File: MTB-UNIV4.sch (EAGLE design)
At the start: 116 parts, among them IC1 MEGA128-A, IC2 SN75176BP, IC3 MC7805CDTG, IC4 ULN2803A, IC5 ULN2803A, Q1 14.745 MHz, X1A MVE252-5-V, X1B MVE252-5-V, X2A MVE252-5-V, X2B MVE252-5-V, X3 1751316, X4 1751316, X5 1751316, X6 1751316

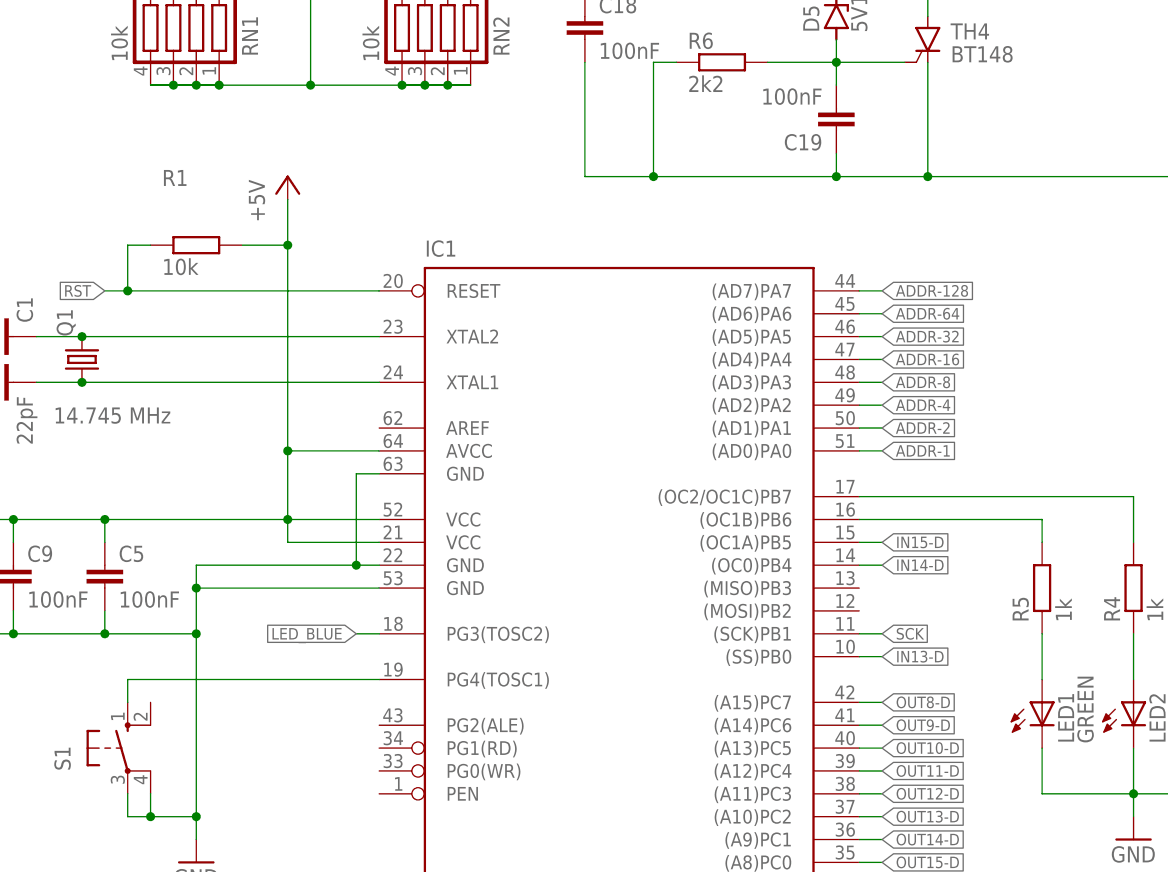
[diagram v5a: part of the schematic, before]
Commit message: Add test pads for MOSI & MISO.
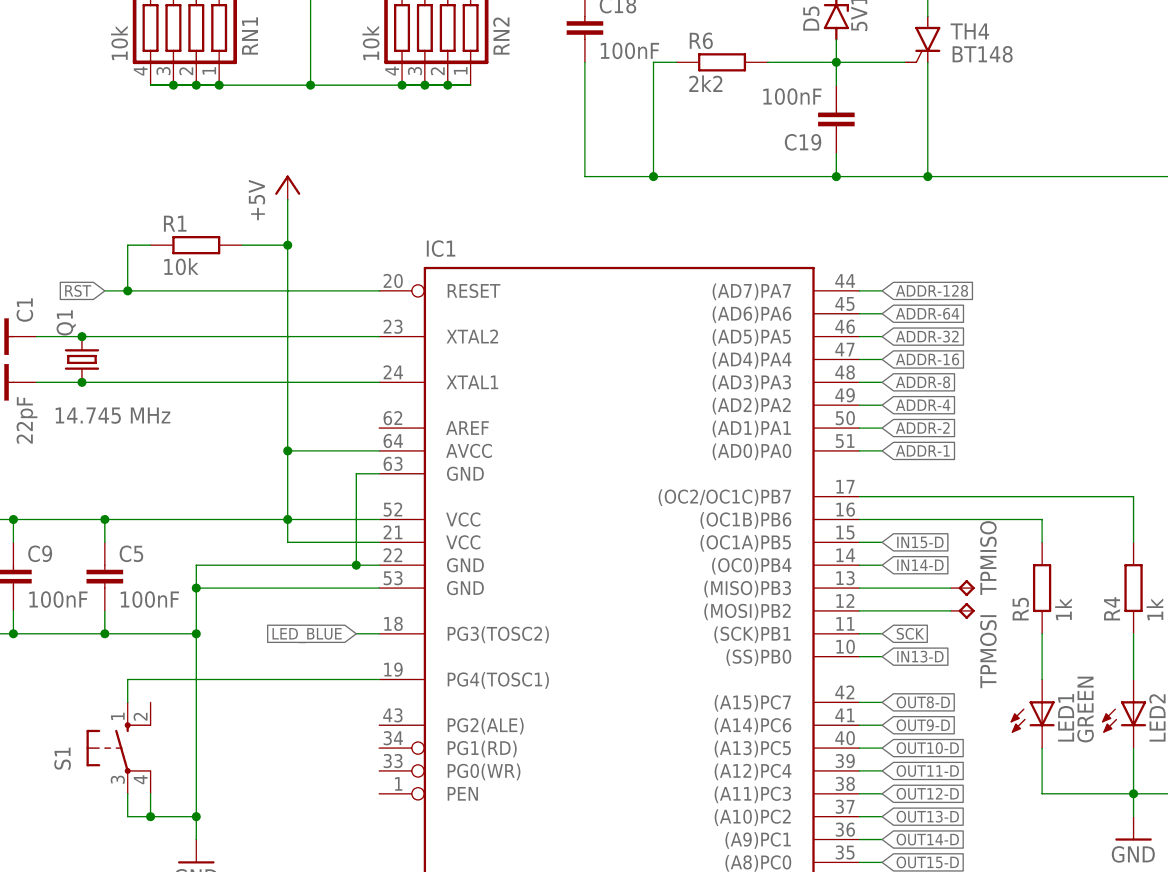
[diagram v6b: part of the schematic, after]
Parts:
- added TPMISO, TPMOSI: TPTP10R, testpad:TPTP10R
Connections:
- new net MISO: IC1.(MISO)PB3, TPMISO.TP
- new net MOSI: IC1.(MOSI)PB2, TPMOSI.TP
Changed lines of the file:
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@@
 <grid distance="0.1" unitdist="inch" unit="inch" style="lines" multiple="1" display="no" altdistance="0.01" altunitdist="inch" altunit="inch"/>
 <layers>
-<layer number="1" name="Top" color="3" fill="1" visible="yes" active="no"/>
-<layer number="2" name="Route2" color="1" fill="3" visible="yes" active="no"/>
-<layer number="3" name="Route3" color="4" fill="3" visible="yes" active="no"/>
-<layer number="4" name="Route4" color="1" fill="4" visible="yes" active="no"/>
-<layer number="5" name="Route5" color="4" fill="4" visible="yes" active="no"/>
-<layer number="6" name="Route6" color="1" fill="8" visible="yes" active="no"/>
-<layer number="7" name="Route7" color="4" fill="8" visible="yes" active="no"/>
-<layer number="8" name="Route8" color="1" fill="2" visible="yes" active="no"/>
-<layer number="9" name="Route9" color="4" fill="2" visible="yes" active="no"/>
-<layer number="10" name="Route10" color="1" fill="7" visible="yes" active="no"/>
-<layer number="11" name="Route11" color="4" fill="7" visible="yes" active="no"/>
-<layer number="12" name="Route12" color="1" fill="5" visible="yes" active="no"/>
-<layer number="13" name="Route13" color="4" fill="5" visible="yes" active="no"/>
-<layer number="14" name="Route14" color="1" fill="6" visible="yes" active="no"/>
-<layer number="15" name="Route15" color="4" fill="6" visible="yes" active="no"/>
-<layer number="16" name="Bottom" color="4" fill="1" visible="yes" active="no"/>
-<layer number="17" name="Pads" color="2" fill="1" visible="yes" active="no"/>
-<layer number="18" name="Vias" color="2" fill="1" visible="yes" active="no"/>
-<layer number="19" name="Unrouted" color="6" fill="1" visible="yes" active="no"/>
-<layer number="20" name="Dimension" color="24" fill="1" visible="yes" active="no"/>
-<layer number="21" name="tPlace" color="7" fill="1" visible="yes" active="no"/>
-<layer number="22" name="bPlace" color="7" fill="1" visible="yes" active="no"/>
-<layer number="23" name="tOrigins" color="15" fill="1" visible="yes" active="no"/>
-<layer number="24" name="bOrigins" color="15" fill="1" visible="yes" active="no"/>
-<layer number="25" name="tNames" color="7" fill="1" visible="yes" active="no"/>
-<layer number="26" name="bNames" color="7" fill="1" visible="yes" active="no"/>
-<layer number="27" name="tValues" color="7" fill="1" visible="yes" active="no"/>
-<layer number="28" name="bValues" color="7" fill="1" visible="yes" active="no"/>
+<layer number="1" name="Top" color="3" fill="1" visible="no" active="no"/>
+<layer number="2" name="Route2" color="1" fill="3" visible="no" active="no"/>
+<layer number="3" name="Route3" color="4" fill="3" visible="no" active="no"/>
+<layer number="4" name="Route4" color="1" fill="4" visible="no" active="no"/>
+<layer number="5" name="Route5" color="4" fill="4" visible="no" active="no"/>
+<layer number="6" name="Route6" color="1" fill="8" visible="no" active="no"/>
+<layer number="7" name="Route7" color="4" fill="8" visible="no" active="no"/>
+<layer number="8" name="Route8" color="1" fill="2" visible="no" active="no"/>
+<layer number="9" name="Route9" color="4" fill="2" visible="no" active="no"/>
+<layer number="10" name="Route10" color="1" fill="7" visible="no" active="no"/>
+<layer number="11" name="Route11" color="4" fill="7" visible="no" active="no"/>
+<layer number="12" name="Route12" color="1" fill="5" visible="no" active="no"/>
+<layer number="13" name="Route13" color="4" fill="5" visible="no" active="no"/>
+<layer number="14" name="Route14" color="1" fill="6" visible="no" active="no"/>
+<layer number="15" name="Route15" color="4" fill="6" visible="no" active="no"/>
+<layer number="16" name="Bottom" color="4" fill="1" visible="no" active="no"/>
+<layer number="17" name="Pads" color="2" fill="1" visible="no" active="no"/>
+<layer number="18" name="Vias" color="2" fill="1" visible="no" active="no"/>
+<layer number="19" name="Unrouted" color="6" fill="1" visible="no" active="no"/>
+<layer number="20" name="Dimension" color="24" fill="1" visible="no" active="no"/>
+<layer number="21" name="tPlace" color="7" fill="1" visible="no" active="no"/>
+<layer number="22" name="bPlace" color="7" fill="1" visible="no" active="no"/>
+<layer number="23" name="tOrigins" color="15" fill="1" visible="no" active="no"/>
+<layer number="24" name="bOrigins" color="15" fill="1" visible="no" active="no"/>
+<layer number="25" name="tNames" color="7" fill="1" visible="no" active="no"/>
+<layer number="26" name="bNames" color="7" fill="1" visible="no" active="no"/>
+<layer number="27" name="tValues" color="7" fill="1" visible="no" active="no"/>
+<layer number="28" name="bValues" color="7" fill="1" visible="no" active="no"/>
 <layer number="29" name="tStop" color="7" fill="3" visible="no" active="no"/>
 <layer number="30" name="bStop" color="7" fill="6" visible="no" active="no"/>
@@
 <layer number="35" name="tGlue" color="7" fill="4" visible="no" active="no"/>
 <layer number="36" name="bGlue" color="7" fill="5" visible="no" active="no"/>
-<layer number="37" name="tTest" color="7" fill="1" visible="yes" active="no"/>
-<layer number="38" name="bTest" color="7" fill="1" visible="yes" active="no"/>
+<layer number="37" name="tTest" color="7" fill="1" visible="no" active="no"/>
+<layer number="38" name="bTest" color="7" fill="1" visible="no" active="no"/>
 <layer number="39" name="tKeepout" color="4" fill="11" visible="no" active="no"/>
 <layer number="40" name="bKeepout" color="1" fill="11" visible="no" active="no"/>
@@
 <layer number="44" name="Drills" color="7" fill="1" visible="no" active="no"/>
 <layer number="45" name="Holes" color="7" fill="1" visible="no" active="no"/>
-<layer number="46" name="Milling" color="3" fill="1" visible="yes" active="no"/>
-<layer number="47" name="Measures" color="7" fill="1" visible="yes" active="no"/>
-<layer number="48" name="Document" color="7" fill="1" visible="yes" active="no"/>
-<layer number="49" name="Reference" color="7" fill="1" visible="yes" active="no"/>
-<layer number="50" name="dxf" color="7" fill="1" visible="yes" active="no"/>
-<layer number="51" name="tDocu" color="7" fill="1" visible="yes" active="no"/>
-<layer number="52" name="bDocu" color="7" fill="1" visible="yes" active="no"/>
-<layer number="53" name="tGND_GNDA" color="7" fill="9" visible="yes" active="no"/>
-<layer number="54" name="bGND_GNDA" color="1" fill="9" visible="yes" active="no"/>
-<layer number="56" name="wert" color="7" fill="1" visible="yes" active="no"/>
-<layer number="57" name="tCAD" color="7" fill="1" visible="yes" active="no"/>
-<layer number="59" name="tCarbon" color="7" fill="1" visible="yes" active="no"/>
-<layer number="60" name="bCarbon" color="7" fill="1" visible="yes" active="no"/>
+<layer number="46" name="Milling" color="3" fill="1" visible="no" active="no"/>
+<layer number="47" name="Measures" color="7" fill="1" visible="no" active="no"/>
+<layer number="48" name="Document" color="7" fill="1" visible="no" active="no"/>
+<layer number="49" name="Reference" color="7" fill="1" visible="no" active="no"/>
+<layer number="50" name="dxf" color="7" fill="1" visible="no" active="no"/>
+<layer number="51" name="tDocu" color="7" fill="1" visible="no" active="no"/>
+<layer number="52" name="bDocu" color="7" fill="1" visible="no" active="no"/>
+<layer number="53" name="tGND_GNDA" color="7" fill="9" visible="no" active="no"/>
+<layer number="54" name="bGND_GNDA" color="1" fill="9" visible="no" active="no"/>
+<layer number="56" name="wert" color="7" fill="1" visible="no" active="no"/>
+<layer number="57" name="tCAD" color="7" fill="1" visible="no" active="no"/>
+<layer number="59" name="tCarbon" color="7" fill="1" visible="no" active="no"/>
+<layer number="60" name="bCarbon" color="7" fill="1" visible="no" active="no"/>
 <layer number="88" name="SimResults" color="9" fill="1" visible="yes" active="yes"/>
 <layer number="89" name="SimProbes" color="9" fill="1" visible="yes" active="yes"/>
@@
 <attribute name="LCSC_PART" value="C45783"/>
 </part>
+<part name="TPMISO" library="testpad" library_urn="urn:adsk.eagle:library:385" deviceset="TP" device="TP10R" package3d_urn="urn:adsk.eagle:package:27959/1" value="TPTP10R"/>
+<part name="TPMOSI" library="testpad" library_urn="urn:adsk.eagle:library:385" deviceset="TP" device="TP10R" package3d_urn="urn:adsk.eagle:package:27959/1" value="TPTP10R"/>
 </parts>
 <sheets>
@@
 </instance>
 <instance part="R1" gate="G$1" x="48.26" y="127" smashed="yes">
-<attribute name="NAME" x="44.45" y="133.5786" size="1.778" layer="95"/>
+<attribute name="NAME" x="44.45" y="128.4986" size="1.778" layer="95"/>
 <attribute name="VALUE" x="44.45" y="123.698" size="1.778" layer="96"/>
 <attribute name="LCSC_PART" x="48.26" y="127" size="1.778" layer="96" display="off"/>
@@
 <attribute name="LCSC_PART" x="325.12" y="66.04" size="1.778" layer="96" rot="MR0" display="off"/>
 </instance>
+<instance part="TPMISO" gate="G$1" x="134.62" y="88.9" smashed="yes" rot="R270">
+<attribute name="NAME" x="137.16" y="88.138" size="1.778" layer="95" rot="R90"/>
+<attribute name="TP_SIGNAL_NAME" x="133.35" y="87.63" size="1.778" layer="97" rot="R270"/>
+</instance>
+<instance part="TPMOSI" gate="G$1" x="134.62" y="86.36" smashed="yes" rot="R270">
+<attribute name="NAME" x="135.382" y="86.106" size="1.778" layer="95" rot="R270"/>
+<attribute name="TP_SIGNAL_NAME" x="133.35" y="85.09" size="1.778" layer="97" rot="R270"/>
+</instance>
 </instances>
 <busses>
@@
 </segment>
 </net>
+<net name="MISO" class="0">
+<segment>
+<pinref part="TPMISO" gate="G$1" pin="TP"/>
+<pinref part="IC1" gate="G$1" pin="(MISO)PB3"/>
+<wire x1="132.08" y1="88.9" x2="121.92" y2="88.9" width="0.1524" layer="91"/>
+</segment>
+</net>
+<net name="MOSI" class="0">
+<segment>
+<pinref part="IC1" gate="G$1" pin="(MOSI)PB2"/>
+<pinref part="TPMOSI" gate="G$1" pin="TP"/>
+<wire x1="121.92" y1="86.36" x2="132.08" y2="86.36" width="0.1524" layer="91"/>
+</segment>
+</net>

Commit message: Add AREF 100nF capacitor.
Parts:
- added C11: 100nF, rcl:C-EUC0805
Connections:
- new net AREF: C11.1, IC1.AREF
- net GND: now also C11.2
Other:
- note added: "v4.3"
- note removed: "v4.2"
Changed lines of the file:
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@@
 <part name="TPMISO" library="testpad" library_urn="urn:adsk.eagle:library:385" deviceset="TP" device="TP10R" package3d_urn="urn:adsk.eagle:package:27959/1" value="TPTP10R"/>
 <part name="TPMOSI" library="testpad" library_urn="urn:adsk.eagle:library:385" deviceset="TP" device="TP10R" package3d_urn="urn:adsk.eagle:package:27959/1" value="TPTP10R"/>
+<part name="C11" library="rcl" deviceset="C-EU" device="C0805" value="100nF"/>
 </parts>
 <sheets>
@@
 KMŽ Brno I, LRKV MENDELU
 2020-2021</text>
-<text x="375.158" y="5.08" size="2.54" layer="94">v4.2</text>
+<text x="375.158" y="5.08" size="2.54" layer="94">v4.3</text>
 <text x="344.17" y="20.32" size="2.54" layer="94">All</text>
 <text x="335.28" y="25.4" size="1.9304" layer="97" align="bottom-center">Released under the Creative Commons Attribution-ShareAlike 4.0 License
@@
 <attribute name="VALUE" x="165.862" y="85.09" size="1.778" layer="96" rot="R90"/>
 </instance>
-<instance part="GND8" gate="1" x="20.32" y="106.68" smashed="yes">
-<attribute name="VALUE" x="17.78" y="104.14" size="1.778" layer="96"/>
+<instance part="GND8" gate="1" x="20.32" y="101.6" smashed="yes">
+<attribute name="VALUE" x="17.78" y="99.06" size="1.778" layer="96"/>
 </instance>
 <instance part="C6" gate="G$1" x="325.12" y="66.04" smashed="yes" rot="MR0">
@@
 <attribute name="TP_SIGNAL_NAME" x="133.35" y="85.09" size="1.778" layer="97" rot="R270"/>
 </instance>
+<instance part="C11" gate="G$1" x="53.34" y="106.68" smashed="yes" rot="R270">
+<attribute name="NAME" x="53.721" y="105.156" size="1.778" layer="95" rot="R270"/>
+<attribute name="VALUE" x="48.641" y="105.156" size="1.778" layer="96" rot="R270"/>
+</instance>
 </instances>
 <busses>
@@
 <segment>
 <pinref part="GND8" gate="1" pin="GND"/>
-<wire x1="20.32" y1="109.22" x2="20.32" y2="111.76" width="0.1524" layer="91"/>
+<wire x1="20.32" y1="104.14" x2="20.32" y2="106.68" width="0.1524" layer="91"/>
 <pinref part="C2" gate="G$1" pin="1"/>
+<wire x1="20.32" y1="106.68" x2="20.32" y2="111.76" width="0.1524" layer="91"/>
 <wire x1="20.32" y1="111.76" x2="22.86" y2="111.76" width="0.1524" layer="91"/>
 <wire x1="20.32" y1="111.76" x2="20.32" y2="116.84" width="0.1524" layer="91"/>
@@
 <pinref part="C1" gate="G$1" pin="2"/>
 <wire x1="20.32" y1="116.84" x2="22.86" y2="116.84" width="0.1524" layer="91"/>
+<pinref part="C11" gate="G$1" pin="2"/>
+<wire x1="48.26" y1="106.68" x2="20.32" y2="106.68" width="0.1524" layer="91"/>
+<junction x="20.32" y="106.68"/>
 </segment>
 </net>
@@
 </segment>
 </net>
+<net name="AREF" class="0">
+<segment>
+<pinref part="C11" gate="G$1" pin="1"/>
+<pinref part="IC1" gate="G$1" pin="AREF"/>
+<wire x1="55.88" y1="106.68" x2="68.58" y2="106.68" width="0.1524" layer="91"/>
+</segment>
+</net>
